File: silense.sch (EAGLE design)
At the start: 192 parts, among them IC1 AD8334ACPZ, J1 FMC-LPC

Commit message: AD8334 WIP
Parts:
- C10, C5, C8, C9: value o.1uF -> 0.1uF
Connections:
- net INH3: now also IC1.INH3
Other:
- note added: "Channel 1,2"
- moved on the sheet: C10, C11, C12, C13, C14, C15, C16, C17, C18, C19, C20, C23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

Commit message: WIP AD8334
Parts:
- added C1, C2, C3, C4, C6, C7: 0.1uF, Wurth_Elektronik_Passive_Capacitors_rev18b:WCAP-CSGP_0402_885012205037
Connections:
- removed net INH3: C23.1, C24.2, C25.1, IC1.INH3
- removed net LO3_N: R6.1
- removed net LO4_N: R7.1
- removed net R2_1: IC1.INH2
- new net INH2: C23.1, C24.2, C25.1, IC1.INH2
- new net N$15: C12.1
- net GND: now also C5.2; no longer C5.1
- net INH4: now also IC1.INH3
- net N$1: now also C5.1; no longer C5.2
- net R1_LO_N: now also C1.1, IC1.LON3, R7.1; no longer C12.1
- net R1_LO_P: now also C2.1, IC1.LOP3
- net R1_V2I_N: now also C1.2
- net R1_V2I_P: now also C2.2
- net R1_V2O_N: now also C4.1
- net R1_V2O_P: now also C3.1
- net R2_LO_N: now also R6.1
- net R2_V2O_N: now also C6.1
- net R2_V2O_P: now also C7.1
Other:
- note added: "TODO change impedance matching values"
- note added: "TODO make ground symbols the same"
- moved on the sheet: C11, C12, C13, C14, C15, C16, C17, C18, C21, C22, C25, C26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

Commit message: update: - some more todos - output connector added - input connections (16 channels)
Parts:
- removed U$1: HIROSE_FH28-68S-05SH05, wouter:HIROSE_FH28-68S-05SH05
- added C30: CBEC219-3479B001C1AF, wouter:CBEC219-3479B001C1AF
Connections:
- new net 3P3V: J1C.3P3V@3, J1D.3P3V@2
- new net IN0_0: J1G.LA00_P_CC, STHV_0.IN1_0
- new net IN0_1: J1G.LA00_N_CC, STHV_0.IN1_1
- new net IN10_0: J1G.LA20_P
- new net IN10_1: J1G.LA20_N
- new net IN11_0: J1H.LA19_P
- new net IN11_1: J1H.LA19_N
- new net IN12_0: J1G.LA22_P
- new net IN12_1: J1G.LA22_N
- new net IN13_0: J1H.LA21_P
- new net IN13_1: J1H.LA21_N
- new net IN14_0: J1G.LA25_P
- new net IN14_1: J1G.LA25_N
- new net IN15_0: J1H.LA24_P
- new net IN15_1: J1H.LA24_N
- new net IN9_0: J1H.LA15_P
- new net IN9_1: J1H.LA15_N
- new net LA28_N: J1H.LA28_N
- new net LA28_P: J1H.LA28_P
- new net LA30_N: J1H.LA30_N
- new net LA30_P: J1H.LA30_P
- new net LA32_N: J1H.LA32_N
- new net LA32_P: J1H.LA32_P
- new net OUT_10: C30.12
- new net OUT_11: C30.13
- new net OUT_12: C30.14
- new net OUT_13: C30.15
- new net OUT_14: C30.16
- new net OUT_15: C30.17
- new net OUT_16: C30.18
- new net OUT_17: C30.19
- new net OUT_18: C30.20
- new net OUT_19: C30.21
- new net OUT_20: C30.22
- new net OUT_21: C30.23
- new net OUT_22: C30.24
- new net OUT_23: C30.25
- new net OUT_24: C30.26
- new net OUT_25: C30.27
- new net OUT_26: C30.28
- new net OUT_27: C30.29
- new net OUT_28: C30.30
- new net OUT_29: C30.31
- new net OUT_30: C30.32
- new net OUT_31: C30.33
- new net OUT_32: C30.36
- new net OUT_33: C30.37
- new net OUT_34: C30.38
- new net OUT_35: C30.39
- new net OUT_36: C30.40
- new net OUT_37: C30.41
- new net OUT_38: C30.42
- new net OUT_39: C30.43
- new net OUT_40: C30.44
- new net OUT_41: C30.45
- new net OUT_42: C30.46
- new net OUT_43: C30.47
- new net OUT_44: C30.48
- new net OUT_45: C30.49
- new net OUT_46: C30.50
- new net OUT_47: C30.51
- new net OUT_48: C30.52
- new net OUT_49: C30.53
- new net OUT_50: C30.54
- new net OUT_51: C30.55
- new net OUT_52: C30.56
- new net OUT_53: C30.57
- new net OUT_54: C30.58
- new net OUT_55: C30.59
- new net OUT_56: C30.60
- new net OUT_57: C30.61
- new net OUT_58: C30.62
- new net OUT_59: C30.63
- new net OUT_60: C30.64
- new net OUT_61: C30.65
- new net OUT_62: C30.66
- new net OUT_63: C30.67
- new net OUT_8: C30.10
- new net OUT_9: C30.11
- net GND: now also C30.1, C30.34, C30.35, C30.68, J1C.GND@41, J1C.GND@42, J1C.GND@43, J1C.GND@44, J1C.GND@45, J1C.GND@46, J1C.GND@47, J1C.GND@48, J1C.GND@49, J1C.GND@50, J1C.GND@51, J1C.GND@52, J1C.GND@53, J1C.GND@54, J1C.GND@55, J1C.GND@56, J1C.GND@57, J1C.GND@58, J1C.GND@59, J1C.GND@60, J1D.GND@28, J1D.GND@29, J1D.GND@30, J1D.GND@31, J1D.GND@32, J1D.GND@33, J1D.GND@34, J1D.GND@35, J1D.GND@36, J1D.GND@37, J1D.GND@38, J1D.GND@39, J1D.GND@40, J1G.GND@13, J1G.GND@14, J1G.GND@15, J1G.GND@16, J1G.GND@17, J1G.GND@18, J1G.GND@19, J1G.GND@20, J1G.GND@21, J1G.GND@22, J1G.GND@23, J1G.GND@24, J1G.GND@25, J1G.GND@26, J1G.GND@27, J1H.GND, J1H.GND@1, J1H.GND@10, J1H.GND@11, J1H.GND@12, J1H.GND@2, J1H.GND@3, J1H.GND@4, J1H.GND@5, J1H.GND@6, J1H.GND@7, J1H.GND@8, J1H.GND@9
- net IN1_0: now also J1H.LA02_P, STHV_0.IN2_0
- net IN1_1: now also J1H.LA02_N, STHV_0.IN2_1
- net IN2_0: now also J1G.LA03_P, STHV_0.IN3_0
- net IN2_1: now also J1G.LA03_N, STHV_0.IN3_1
- net IN3_0: now also J1H.LA04_P, STHV_0.IN4_0
- net IN3_1: now also J1H.LA04_N, STHV_0.IN4_1
- net IN4_0: now also J1G.LA08_P, STHV_0.IN5_0
- net IN4_1: now also J1G.LA08_N, STHV_0.IN5_1
- net IN5_0: now also J1H.LA07_P, STHV_0.IN6_0
- net IN5_1: now also J1H.LA07_N, STHV_0.IN6_1
- net IN6_0: now also J1G.LA12_P, STHV_0.IN7_0
- net IN6_1: now also J1G.LA12_N, STHV_0.IN7_1
- net IN7_0: now also J1H.LA11_P, STHV_0.IN8_0
- net IN7_1: now also J1H.LA11_N, STHV_0.IN8_1
- net IN8_0: now also J1G.LA16_P
- net IN8_1: now also J1G.LA16_N
- net OUT_0: now also C30.2
- net OUT_1: now also C30.3
- net OUT_2: now also C30.4
- net OUT_3: now also C30.5
- net OUT_4: now also C30.6
- net OUT_5: now also C30.7
- net OUT_6: now also C30.8
- net OUT_7: now also C30.9
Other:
- note added: "TODO: add the same once more for 16 channels TODO: separate inx_1"
- note added: "todo: @wouter check if LA00_N_CC is usable pin"
- note added: "todo: alle 3v3 met elkaar verbinden (ook van powerboard?)"
- note added: "todo: check 5V: is it necessary or 3v3 also fine? => 3v3 comes from zedboard as well as powerconnboard"

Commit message: added powerblock for +-5V
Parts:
- added C39: C3216X7R1H225K160AE, samacsys:C3216X7R1H225K160AE
- added C40, C43, C44, C47: 1206 x7r 47uF 25V, samacsys:CKG57NX5R1E476M500JH
- added C41, C42: 0.1uF x7r 1206, samacsys:MCSH31B104K500CT
- added C45, C46: 1206 x7r 2.2uF 25V, rcl:C-EUC1206
- added D25: MBRS360T3G, samacsys:MBRS360T3G
- added D26: VS-MBRS340-M3_9AT, samacsys:VS-MBRS340-M3_9AT
- added IC3: LT8471EFE#PBF, samacsys:LT8471EFE#PBF
- added L2: 744025150, samacsys:744025150
- added L7: 74437324068, samacsys:74437324068
- added L8: 74437324100, samacsys:74437324100
- added R17: 261k 25V, resistor:R-EU_M1206
- added R18: 82k 25V, resistor:R-EU_M1206
- added R19, R21: 316k, rcl:R-EU_R1206
- added R20, R22: 59k, rcl:R-EU_R1206
- added R23, R24: 100k, rcl:R-EU_R1206
- added R25: 187k, rcl:R-EU_R1206
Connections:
- new net C3: IC3.C3, L2.1
- new net E1: D26.K, IC3.E1, L7.1
- new net E2: D25.K, IC3.E2, L8.2
- new net FB1: IC3.FB1, R19.1, R20.2
- new net FB2: IC3.FB2, R21.1, R22.2
- new net N3V3: C44.2, D25.A, R21.2
- new net OV/UV: IC3.OV/UV, R17.2
- new net P3V3: C43.2, L7.2, R19.2
- new net PG1: IC3.PG1, R24.1
- new net PG2: IC3.PG2, R23.2
- new net RT: IC3.RT, R25.1
- new net SS1: C41.2, IC3.SS1
- new net SS2: C42.1, IC3.SS2
- new net VINPOS: C40.2, C45.1, C46.2, IC3.C1, IC3.C2, L2.2, R17.1, R18.2, R23.1, R24.2
- new net VINT: C39.1, C47.1, IC3.SHOUT, IC3.VIN1, IC3.VIN2
- net GND: now also C39.2, C40.1, C41.1, C42.2, C43.1, C44.1, C45.2, C46.1, C47.2, D26.A, IC3.EP, IC3.GND_1, IC3.GND_2, IC3.GND_3, IC3.SYNC, L8.1, R18.1, R20.1, R22.1, R25.2
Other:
- note added: "3V3 deduction"
- note added: "todo: be able to switch between 3.3 and 5v?"

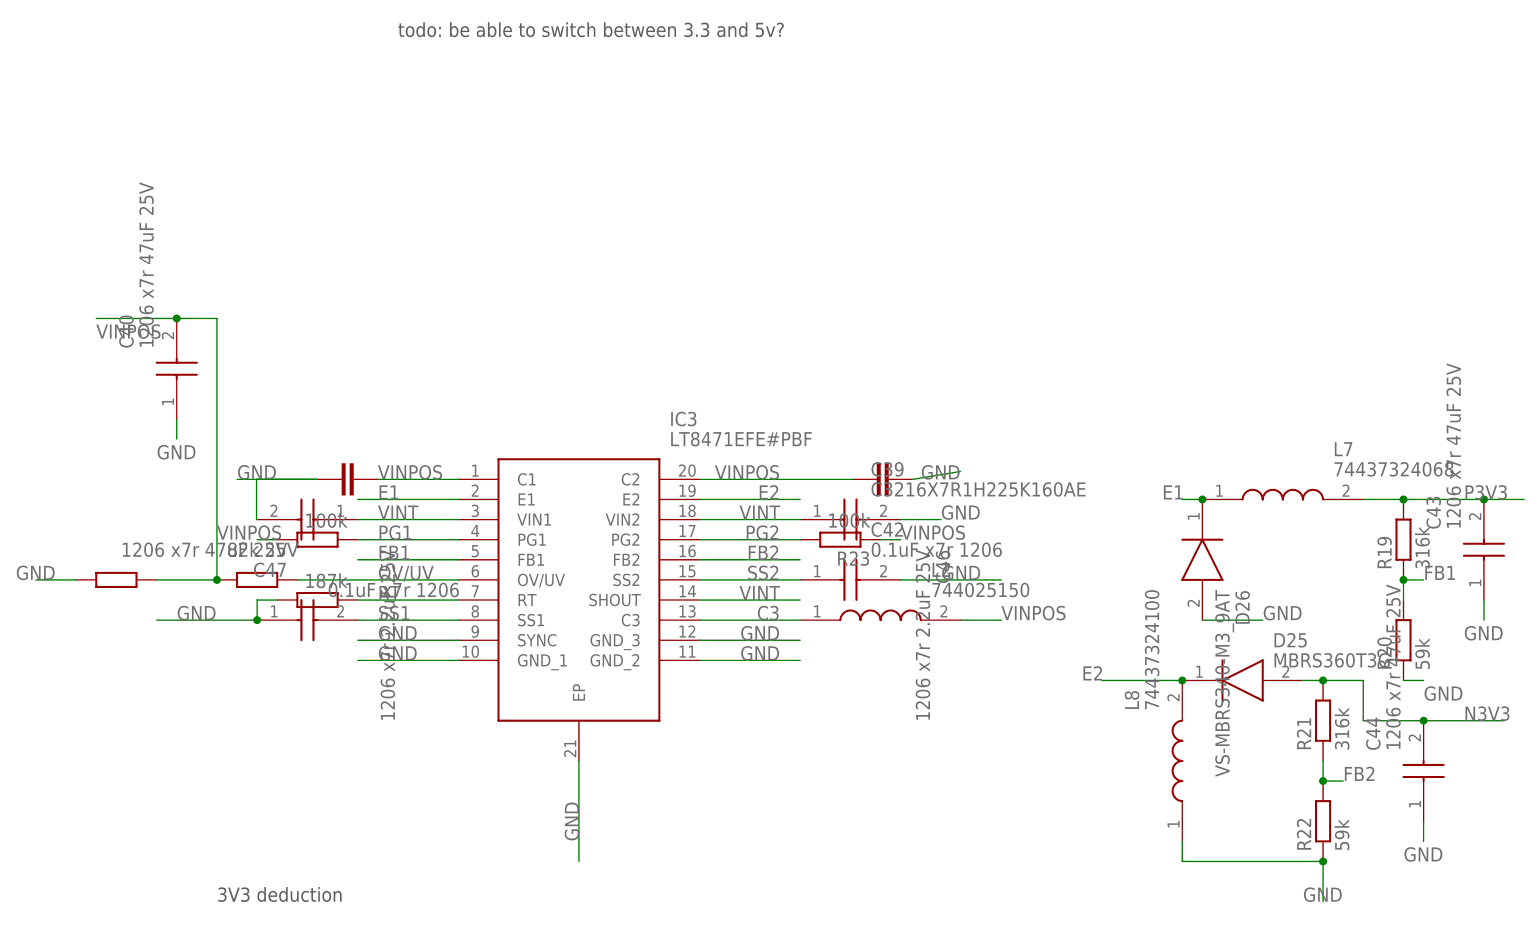
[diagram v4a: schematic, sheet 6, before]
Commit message: updated values and connections for +-5V
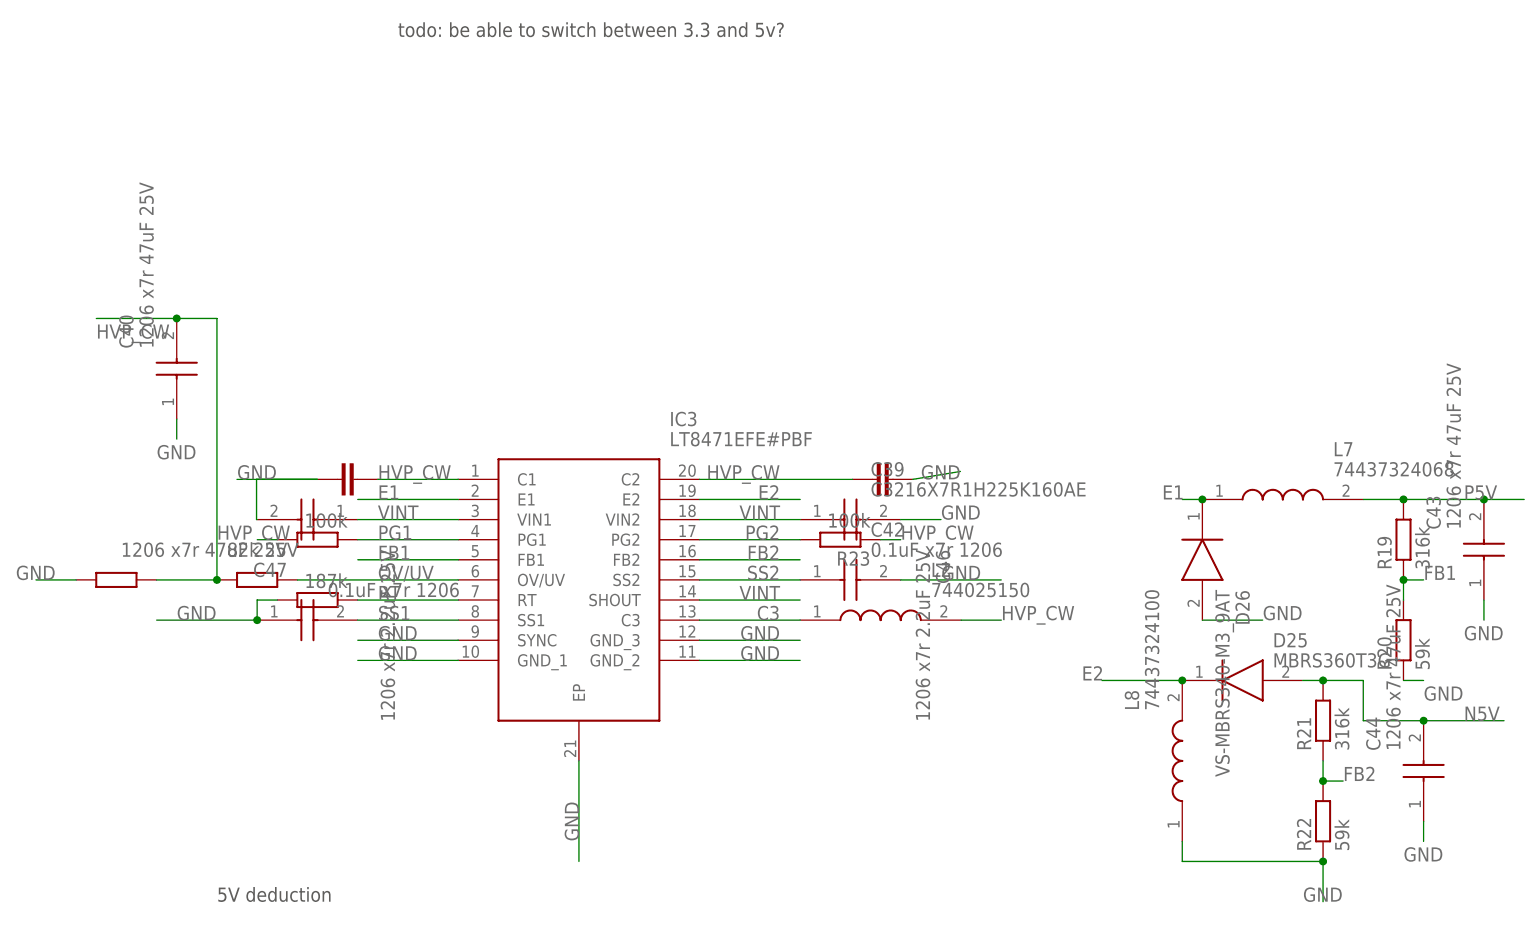
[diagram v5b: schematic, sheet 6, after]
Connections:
- net N3V3 renamed N5V
- net P3V3 renamed P5V
- removed net VINPOS: C40.2, C45.1, C46.2, IC3.C1, IC3.C2, L2.2, R17.1, R18.2, R23.1, R24.2
- net HVP_CW: now also C40.2, C45.1, C46.2, IC3.C1, IC3.C2, L2.2, R17.1, R18.2, R23.1, R24.2
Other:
- note added: "5V deduction"
- note removed: "3V3 deduction"
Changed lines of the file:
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@@
 <sheet>
 <plain>
-<text x="38" y="18" size="1.778" layer="97">3V3 deduction</text>
+<text x="38" y="18" size="1.778" layer="97">5V deduction</text>
 <text x="60.86" y="127.22" size="1.778" layer="97">todo: be able to switch between 3.3 and 5v?</text>
 </plain>
@@
 </segment>
 </net>
-<net name="VINPOS" class="2">
-<segment>
-<pinref part="R18" gate="G$1" pin="2"/>
-<pinref part="R17" gate="G$1" pin="1"/>
-<wire x1="30.38" y1="58.64" x2="38" y2="58.64" width="0.1524" layer="91"/>
-<wire x1="38" y1="58.64" x2="38" y2="91.66" width="0.1524" layer="91"/>
-<wire x1="38" y1="91.66" x2="32.92" y2="91.66" width="0.1524" layer="91"/>
-<junction x="38" y="58.64"/>
-<label x="22.76" y="89.12" size="1.778" layer="95"/>
-<pinref part="C40" gate="G$1" pin="2"/>
-<wire x1="32.92" y1="91.66" x2="22.76" y2="91.66" width="0.1524" layer="91"/>
-<junction x="32.92" y="91.66"/>
-</segment>
-<segment>
-<pinref part="L2" gate="G$1" pin="2"/>
-<wire x1="131.98" y1="53.56" x2="137.06" y2="53.56" width="0.1524" layer="91"/>
-<label x="137.06" y="53.56" size="1.778" layer="95"/>
-</segment>
-<segment>
-<pinref part="R24" gate="G$1" pin="2"/>
-<wire x1="45.62" y1="63.72" x2="43.08" y2="63.72" width="0.1524" layer="91"/>
-<label x="38" y="63.72" size="1.778" layer="95"/>
-</segment>
-<segment>
-<pinref part="R23" gate="G$1" pin="1"/>
-<wire x1="121.82" y1="63.72" x2="124.36" y2="63.72" width="0.1524" layer="91"/>
-<label x="124.36" y="63.72" size="1.778" layer="95"/>
-</segment>
-<segment>
-<pinref part="IC3" gate="G$1" pin="C2"/>
-<wire x1="98.96" y1="71.34" x2="118.28" y2="71.34" width="0.1524" layer="91"/>
-<label x="109.12" y="71.34" size="1.778" layer="95" align="bottom-right"/>
-<pinref part="C46" gate="G$1" pin="2"/>
-</segment>
-<segment>
-<pinref part="IC3" gate="G$1" pin="C1"/>
-<wire x1="68.48" y1="71.34" x2="58.32" y2="71.34" width="0.1524" layer="91"/>
-<label x="58.32" y="71.34" size="1.778" layer="95"/>
-<pinref part="C45" gate="G$1" pin="1"/>
-</segment>
-</net>
-<net name="P3V3" class="2">
+<net name="P5V" class="2">
 <segment>
 <pinref part="R19" gate="G$1" pin="2"/>
@@
 </segment>
 </net>
-<net name="N3V3" class="2">
+<net name="N5V" class="2">
 <segment>
 <pinref part="D25" gate="G$1" pin="A"/>
@@
 </segment>
 </net>
+<net name="HVP_CW" class="0">
+<segment>
+<pinref part="R18" gate="G$1" pin="2"/>
+<pinref part="R17" gate="G$1" pin="1"/>
+<wire x1="30.38" y1="58.64" x2="38" y2="58.64" width="0.1524" layer="91"/>
+<wire x1="38" y1="58.64" x2="38" y2="91.66" width="0.1524" layer="91"/>
+<wire x1="38" y1="91.66" x2="32.92" y2="91.66" width="0.1524" layer="91"/>
+<junction x="38" y="58.64"/>
+<label x="22.76" y="89.12" size="1.778" layer="95"/>
+<pinref part="C40" gate="G$1" pin="2"/>
+<wire x1="32.92" y1="91.66" x2="22.76" y2="91.66" width="0.1524" layer="91"/>
+<junction x="32.92" y="91.66"/>
+</segment>
+<segment>
+<pinref part="L2" gate="G$1" pin="2"/>
+<wire x1="131.98" y1="53.56" x2="137.06" y2="53.56" width="0.1524" layer="91"/>
+<label x="137.06" y="53.56" size="1.778" layer="95"/>
+</segment>
+<segment>
+<pinref part="R24" gate="G$1" pin="2"/>
+<wire x1="45.62" y1="63.72" x2="43.08" y2="63.72" width="0.1524" layer="91"/>
+<label x="38" y="63.72" size="1.778" layer="95"/>
+</segment>
+<segment>
+<pinref part="R23" gate="G$1" pin="1"/>
+<wire x1="121.82" y1="63.72" x2="124.36" y2="63.72" width="0.1524" layer="91"/>
+<label x="124.36" y="63.72" size="1.778" layer="95"/>
+</segment>
+<segment>
+<pinref part="IC3" gate="G$1" pin="C2"/>
+<wire x1="98.96" y1="71.34" x2="118.28" y2="71.34" width="0.1524" layer="91"/>
+<label x="109.12" y="71.34" size="1.778" layer="95" align="bottom-right"/>
+<pinref part="C46" gate="G$1" pin="2"/>
+</segment>
+<segment>
+<pinref part="IC3" gate="G$1" pin="C1"/>
+<wire x1="68.48" y1="71.34" x2="58.32" y2="71.34" width="0.1524" layer="91"/>
+<label x="58.32" y="71.34" size="1.778" layer="95"/>
+<pinref part="C45" gate="G$1" pin="1"/>
+</segment>
+</net>

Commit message: added todos
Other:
- note added: "TODO HVP -> HVP_CW"
- note added: "TODO: 5V in: 20V beperking?"
- note added: "TODO: Power supplies"
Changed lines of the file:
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@@
 <?xml version="1.0" encoding="utf-8"?>
 <!DOCTYPE eagle SYSTEM "eagle.dtd">
-<eagle version="9.5.1">
+<eagle version="9.5.0">
 <drawing>
 <settings>
@@
 <setting verticaltext="up"/>
 </settings>
-<grid distance="1" unitdist="mm" unit="mm" style="lines" multiple="1" display="yes" altdistance="0.5" altunitdist="mm" altunit="mm"/>
+<grid distance="0.1" unitdist="inch" unit="inch" style="lines" multiple="1" display="no" altdistance="0.01" altunitdist="inch" altunit="inch"/>
 <layers>
 <layer number="1" name="Top" color="4" fill="1" visible="no" active="no"/>
@@
 <text x="96.52" y="180.34" size="1.778" layer="91">TODO change impedance matching values</text>
 <text x="96.52" y="175.26" size="1.778" layer="91">TODO make ground symbols the same</text>
+<text x="147.32" y="223.52" size="1.778" layer="91">TODO: Power supplies</text>
 </plain>
 <instances>
@@
 <text x="38" y="18" size="1.778" layer="97">5V deduction</text>
 <text x="60.86" y="127.22" size="1.778" layer="97">todo: be able to switch between 3.3 and 5v?</text>
+<text x="78.74" y="106.68" size="1.778" layer="91">TODO HVP -&gt; HVP_CW</text>
+<text x="78.74" y="101.6" size="1.778" layer="91">TODO: 5V in: 20V beperking?</text>
 </plain>
 <instances>
